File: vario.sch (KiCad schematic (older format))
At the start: 177 parts, among them J10 Conn_01x06, J11 Conn_01x04, J12 Conn_01x04, J13 Conn_01x04, J14 Conn_01x03, J15 Conn_01x04, J16 Conn_01x06, J17 Conn_01x06, J18 Conn_01x04, J19 Conn_01x04, J2 Conn_01x02, J20 Conn_01x06, J21 Conn_Coaxial, J22 USB_B_Micro, J23 USB_B_Micro, J24 Micro_SD_Card_Det_Hirose_DM3AT, J3 6339167-3, J6 Conn_01x06, J7 Conn_01x04, J8 Conn_01x04, J9 Conn_01x02, Q1 AO3401A, SW1 SW_MEC_5E, U1 STM32F407VGTx, U10 AMS1117-3.3, U11 HSCMRRN001PD2A3, U12 MS5611-01BA, U13 MAX3232ECPWR, U14 BLE_HM-11, U15 USBLC6-2SC6, U16 USBLC6-2SC6, U17 AMS1117-3.3, U18 HAMMOND_1593W, U2 MP2359DJ-LF-Z, U3 MP2359DJ-LF-Z, U4 L3GD20, U5 MTi-1IMU, U6 FXOS8700, U7 MS5611-01BA, U8 NEO-M9N, U9 TCAN332DR, Y1 16MHz

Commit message: added latest Schematic file.
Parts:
- removed U5: MTi-1IMU, OWN_Parts_:XSens_MTi1_IMU, symbol OWN_Parts_:MTi-1IMU
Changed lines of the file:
@@
-$EndComp
-$Comp
-L OWN_Parts_:MTi-1IMU U5
-U 1 1 5F93C09B
-P 8025 3675
-F 0 "U5" H 8025 4450 50  0000 C CNN
-F 1 "MTi-1IMU" H 8025 4359 50  0000 C CNN
-F 2 "OWN_Parts_:XSens_MTi1_IMU" H 8125 4475 50  0001 C CNN
-F 3 "" H 8125 4475 50  0001 C CNN
-F 4 "512-MTI-1T" H 8025 3675 50  0001 C CNN "Mouser Part Number"
-F 5 "512-MTI-1T" H 8025 3675 50  0001 C CNN "Mouser-Nr.:"
-	1    8025 3675
-	1    0    0    -1
 $EndComp
 $Comp

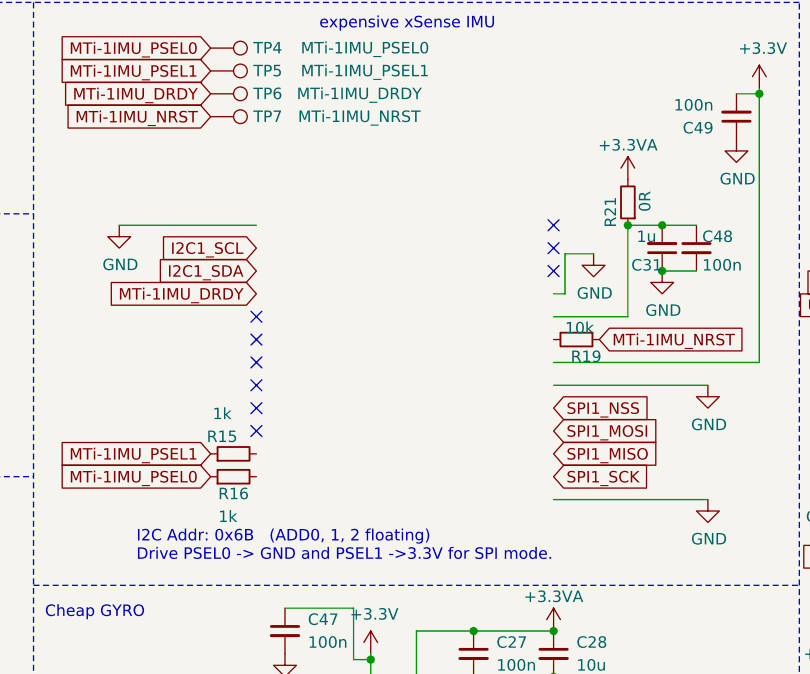
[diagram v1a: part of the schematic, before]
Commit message: readded disapeared XSENSE IMU to schematic.
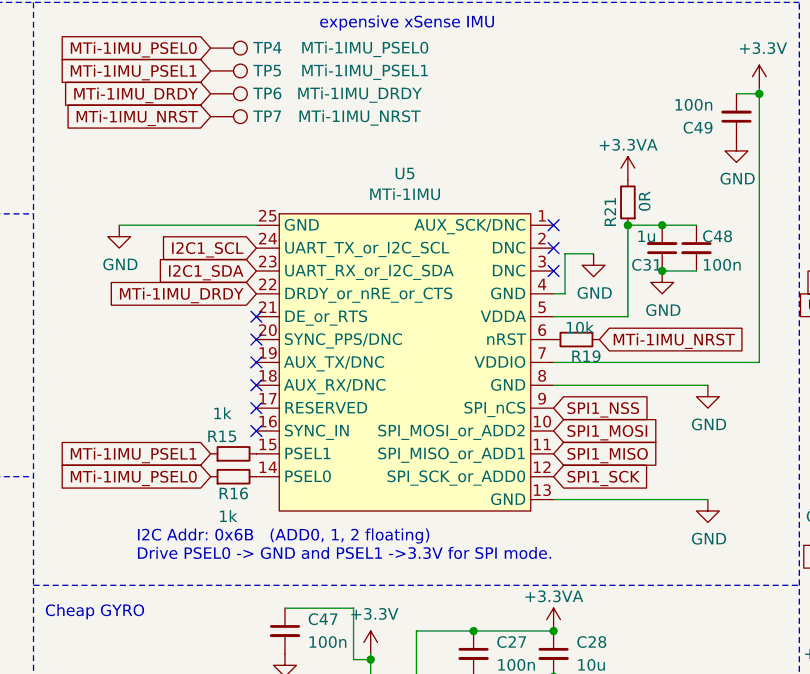
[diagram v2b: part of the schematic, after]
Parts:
- added U5: MTi-1IMU, OWN_Parts_:XSens_MTi1_IMU, symbol OWN_Parts_:MTi-1IMU
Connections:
- net +3V3: now also U5.7 (VDDIO)
- net GND: now also U5.13 (GND), U5.25 (GND), U5.4 (GND), U5.8 (GND)
- net I2C1_SCL: now also U5.24 (UART_TX_or_I2C_SCL)
- net I2C1_SDA: now also U5.23 (UART_RX_or_I2C_SDA)
- net MTi-1IMU_DRDY: now also U5.22 (DRDY_or_nRE_or_CTS)
- net SPI1_MISO: now also U5.11 (SPI_MISO_or_ADD1)
- net SPI1_MOSI: now also U5.10 (SPI_MOSI_or_ADD2)
- net SPI1_NSS: now also U5.9 (SPI_nCS)
- net SPI1_SCK: now also U5.12 (SPI_SCK_or_ADD0)
- net at R19.2: now also U5.6 (nRST)
- net at C31.2, C48.1, R21.1: now also U5.5 (VDDA)
- net at R15.2: now also U5.15 (PSEL1)
- net at R16.2: now also U5.14 (PSEL0)
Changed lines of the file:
@@
 	-1   0    0    1
 $EndComp
+$Comp
+L OWN_Parts_:MTi-1IMU U5
+U 1 1 5FC8D2B4
+P 8025 3675
+F 0 "U5" H 8025 4450 50  0000 C CNN
+F 1 "MTi-1IMU" H 8025 4359 50  0000 C CNN
+F 2 "OWN_Parts_:XSens_MTi1_IMU" H 8125 4475 50  0001 C CNN
+F 3 "" H 8125 4475 50  0001 C CNN
+	1    8025 3675
+	1    0    0    -1
+$EndComp
 $EndSCHEMATC
